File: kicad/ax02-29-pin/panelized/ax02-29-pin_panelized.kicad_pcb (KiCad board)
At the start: 4 copper layers, 100 x 100 mm, 62 parts, among them CN1 Leafony Bus, J2 Conn_02x05_Top_Bottom, J3 Conn_02x05_Top_Bottom, J4 Conn_02x05_Top_Bottom

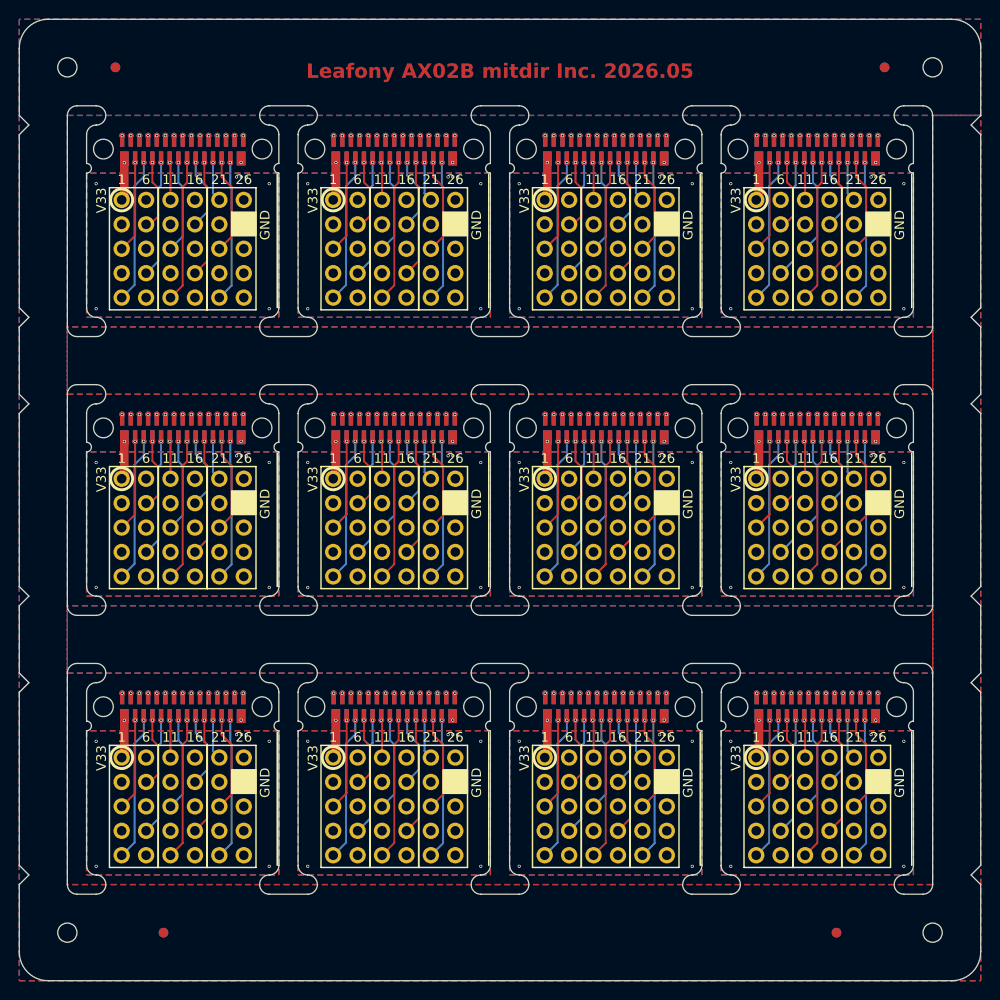
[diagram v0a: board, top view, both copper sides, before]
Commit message: 面付方法を変更
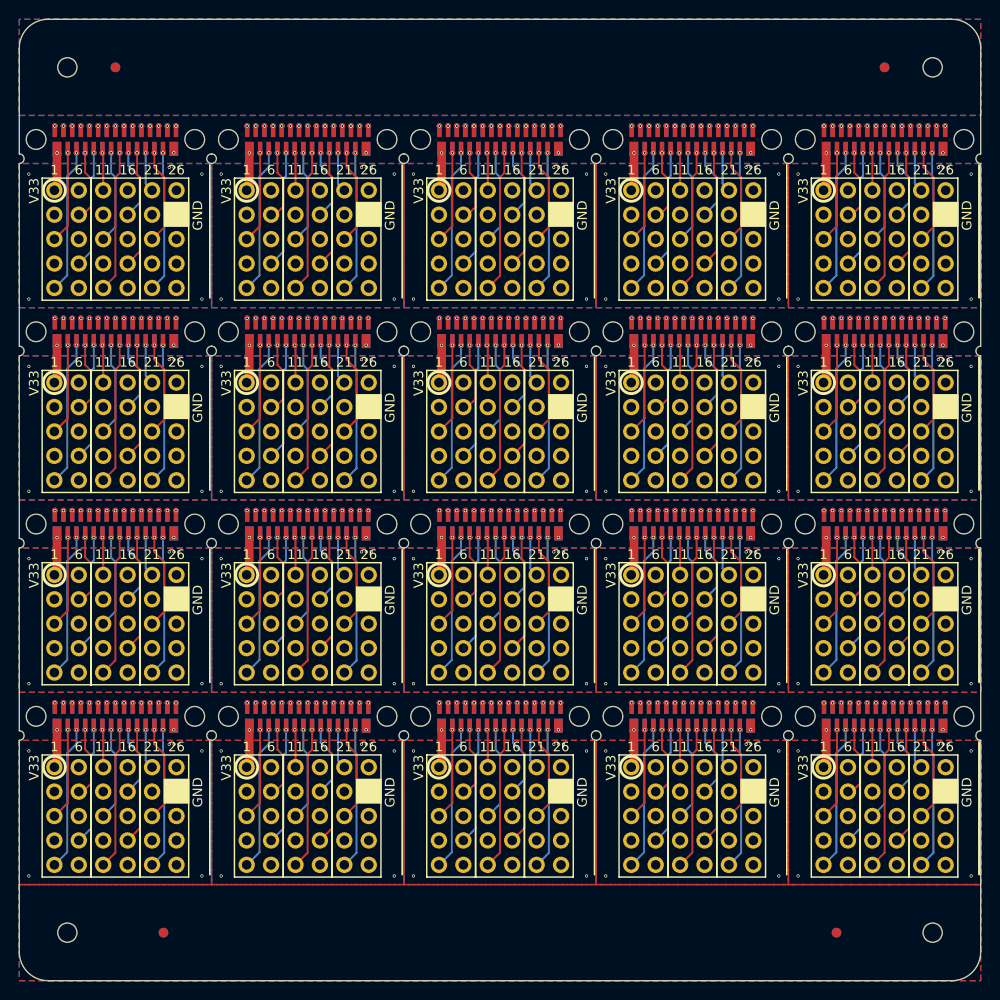
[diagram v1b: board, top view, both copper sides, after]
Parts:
- removed the CN1 at (83.6, 105.3)
- removed the CN1 at (39.6, 105.3)
- removed the CN1 at (105.6, 105.3)
- removed the CN1 at (105.6, 47.3)
- removed the CN1 at (39.6, 76.3)
- removed the CN1 at (61.6, 76.3)
- removed the CN1 at (83.6, 47.3)
- removed the CN1 at (61.6, 105.3)
- removed the CN1 at (83.6, 76.3)
- removed the CN1 at (61.6, 47.3)
- removed the CN1 at (39.6, 47.3)
- removed the CN1 at (105.6, 76.3)
- removed the J2 at (105.3, 109.6)
- removed the J2 at (105.3, 51.6)
- removed the J2 at (39.3, 80.6)
- removed the J2 at (39.3, 109.6)
- removed the J2 at (61.3, 109.6)
- removed the J2 at (83.3, 80.6)
- removed the J2 at (83.3, 109.6)
- removed the J2 at (39.3, 51.6)
- removed the J2 at (61.3, 51.6)
- removed the J2 at (83.3, 51.6)
- removed the J2 at (61.3, 80.6)
- removed the J2 at (105.3, 80.6)
- removed the J3 at (44.4, 80.6)
- removed the J3 at (88.4, 109.6)
- removed the J3 at (110.4, 80.6)
- removed the J3 at (110.4, 51.6)
- removed the J3 at (88.4, 80.6)
- removed the J3 at (66.4, 80.6)
- removed the J3 at (110.4, 109.6)
- removed the J3 at (66.4, 51.6)
- removed the J3 at (66.4, 109.6)
- removed the J3 at (88.4, 51.6)
- removed the J3 at (44.4, 109.6)
- removed the J3 at (44.4, 51.6)
- removed the J4 at (71.5, 80.6)
- removed the J4 at (115.5, 109.6)
- removed the J4 at (71.5, 109.6)
- removed the J4 at (115.5, 51.6)
- removed the J4 at (93.5, 109.6)
- removed the J4 at (49.5, 51.6)
- removed the J4 at (49.5, 109.6)
- removed the J4 at (71.5, 51.6)
- removed the J4 at (93.5, 51.6)
- removed the J4 at (93.5, 80.6)
- removed the J4 at (115.5, 80.6)
- removed the J4 at (49.5, 80.6)
- added CN1: Leafony Bus, Leafony:CN_F29_B29, F.Cu at (32.6, 66.3)
- added CN1: Leafony Bus, Leafony:CN_F29_B29, F.Cu at (112.6, 86.3)
- added CN1: Leafony Bus, Leafony:CN_F29_B29, F.Cu at (112.6, 46.3)
- added CN1: Leafony Bus, Leafony:CN_F29_B29, F.Cu at (32.6, 46.3)
- added CN1: Leafony Bus, Leafony:CN_F29_B29, F.Cu at (72.6, 106.3)
- added CN1: Leafony Bus, Leafony:CN_F29_B29, F.Cu at (72.6, 66.3)
- added CN1: Leafony Bus, Leafony:CN_F29_B29, F.Cu at (52.6, 86.3)
- added CN1: Leafony Bus, Leafony:CN_F29_B29, F.Cu at (92.6, 46.3)
- added CN1: Leafony Bus, Leafony:CN_F29_B29, F.Cu at (112.6, 66.3)
- added CN1: Leafony Bus, Leafony:CN_F29_B29, F.Cu at (92.6, 86.3)
- added CN1: Leafony Bus, Leafony:CN_F29_B29, F.Cu at (92.6, 66.3)
- added CN1: Leafony Bus, Leafony:CN_F29_B29, F.Cu at (32.6, 106.3)
- added CN1: Leafony Bus, Leafony:CN_F29_B29, F.Cu at (92.6, 106.3)
- added CN1: Leafony Bus, Leafony:CN_F29_B29, F.Cu at (52.6, 46.3)
- added CN1: Leafony Bus, Leafony:CN_F29_B29, F.Cu at (72.6, 46.3)
- added CN1: Leafony Bus, Leafony:CN_F29_B29, F.Cu at (112.6, 106.3)
- added CN1: Leafony Bus, Leafony:CN_F29_B29, F.Cu at (52.6, 66.3)
- added CN1: Leafony Bus, Leafony:CN_F29_B29, F.Cu at (32.6, 86.3)
- added CN1: Leafony Bus, Leafony:CN_F29_B29, F.Cu at (72.6, 86.3)
- added CN1: Leafony Bus, Leafony:CN_F29_B29, F.Cu at (52.6, 106.3)
- added J2: Conn_02x05_Top_Bottom, Leafony:PinHeader_2x05_2.54mm, F.Cu at (72.3, 110.6)
- added J2: Conn_02x05_Top_Bottom, Leafony:PinHeader_2x05_2.54mm, F.Cu at (52.3, 110.6)
- added J2: Conn_02x05_Top_Bottom, Leafony:PinHeader_2x05_2.54mm, F.Cu at (112.3, 50.6)
- added J2: Conn_02x05_Top_Bottom, Leafony:PinHeader_2x05_2.54mm, F.Cu at (92.3, 70.6)
- added J2: Conn_02x05_Top_Bottom, Leafony:PinHeader_2x05_2.54mm, F.Cu at (52.3, 70.6)
- added J2: Conn_02x05_Top_Bottom, Leafony:PinHeader_2x05_2.54mm, F.Cu at (112.3, 110.6)
- added J2: Conn_02x05_Top_Bottom, Leafony:PinHeader_2x05_2.54mm, F.Cu at (112.3, 70.6)
- added J2: Conn_02x05_Top_Bottom, Leafony:PinHeader_2x05_2.54mm, F.Cu at (52.3, 90.6)
- added J2: Conn_02x05_Top_Bottom, Leafony:PinHeader_2x05_2.54mm, F.Cu at (92.3, 90.6)
- added J2: Conn_02x05_Top_Bottom, Leafony:PinHeader_2x05_2.54mm, F.Cu at (52.3, 50.6)
- added J2: Conn_02x05_Top_Bottom, Leafony:PinHeader_2x05_2.54mm, F.Cu at (32.3, 110.6)
- added J2: Conn_02x05_Top_Bottom, Leafony:PinHeader_2x05_2.54mm, F.Cu at (72.3, 70.6)
- added J2: Conn_02x05_Top_Bottom, Leafony:PinHeader_2x05_2.54mm, F.Cu at (92.3, 110.6)
- added J2: Conn_02x05_Top_Bottom, Leafony:PinHeader_2x05_2.54mm, F.Cu at (72.3, 90.6)
- added J2: Conn_02x05_Top_Bottom, Leafony:PinHeader_2x05_2.54mm, F.Cu at (72.3, 50.6)
- added J2: Conn_02x05_Top_Bottom, Leafony:PinHeader_2x05_2.54mm, F.Cu at (112.3, 90.6)
- added J2: Conn_02x05_Top_Bottom, Leafony:PinHeader_2x05_2.54mm, F.Cu at (32.3, 70.6)
- added J2: Conn_02x05_Top_Bottom, Leafony:PinHeader_2x05_2.54mm, F.Cu at (92.3, 50.6)
- added J2: Conn_02x05_Top_Bottom, Leafony:PinHeader_2x05_2.54mm, F.Cu at (32.3, 50.6)
- added J2: Conn_02x05_Top_Bottom, Leafony:PinHeader_2x05_2.54mm, F.Cu at (32.3, 90.6)
- added J3: Conn_02x05_Top_Bottom, Leafony:PinHeader_2x05_2.54mm, F.Cu at (97.4, 110.6)
- added J3: Conn_02x05_Top_Bottom, Leafony:PinHeader_2x05_2.54mm, F.Cu at (97.4, 90.6)
- added J3: Conn_02x05_Top_Bottom, Leafony:PinHeader_2x05_2.54mm, F.Cu at (77.4, 50.6)
- added J3: Conn_02x05_Top_Bottom, Leafony:PinHeader_2x05_2.54mm, F.Cu at (117.4, 110.6)
- added J3: Conn_02x05_Top_Bottom, Leafony:PinHeader_2x05_2.54mm, F.Cu at (37.4, 90.6)
- added J3: Conn_02x05_Top_Bottom, Leafony:PinHeader_2x05_2.54mm, F.Cu at (37.4, 50.6)
- added J3: Conn_02x05_Top_Bottom, Leafony:PinHeader_2x05_2.54mm, F.Cu at (117.4, 90.6)
- added J3: Conn_02x05_Top_Bottom, Leafony:PinHeader_2x05_2.54mm, F.Cu at (77.4, 90.6)
- added J3: Conn_02x05_Top_Bottom, Leafony:PinHeader_2x05_2.54mm, F.Cu at (77.4, 70.6)
- added J3: Conn_02x05_Top_Bottom, Leafony:PinHeader_2x05_2.54mm, F.Cu at (57.4, 70.6)
- added J3: Conn_02x05_Top_Bottom, Leafony:PinHeader_2x05_2.54mm, F.Cu at (57.4, 90.6)
- added J3: Conn_02x05_Top_Bottom, Leafony:PinHeader_2x05_2.54mm, F.Cu at (97.4, 50.6)
- added J3: Conn_02x05_Top_Bottom, Leafony:PinHeader_2x05_2.54mm, F.Cu at (37.4, 70.6)
- added J3: Conn_02x05_Top_Bottom, Leafony:PinHeader_2x05_2.54mm, F.Cu at (77.4, 110.6)
- added J3: Conn_02x05_Top_Bottom, Leafony:PinHeader_2x05_2.54mm, F.Cu at (37.4, 110.6)
- added J3: Conn_02x05_Top_Bottom, Leafony:PinHeader_2x05_2.54mm, F.Cu at (97.4, 70.6)
- added J3: Conn_02x05_Top_Bottom, Leafony:PinHeader_2x05_2.54mm, F.Cu at (117.4, 50.6)
- added J3: Conn_02x05_Top_Bottom, Leafony:PinHeader_2x05_2.54mm, F.Cu at (57.4, 110.6)
- added J3: Conn_02x05_Top_Bottom, Leafony:PinHeader_2x05_2.54mm, F.Cu at (57.4, 50.6)
- added J3: Conn_02x05_Top_Bottom, Leafony:PinHeader_2x05_2.54mm, F.Cu at (117.4, 70.6)
- added J4: Conn_02x05_Top_Bottom, Leafony:PinHeader_2x05_2.54mm, F.Cu at (102.5, 50.6)
- added J4: Conn_02x05_Top_Bottom, Leafony:PinHeader_2x05_2.54mm, F.Cu at (62.5, 50.6)
- added J4: Conn_02x05_Top_Bottom, Leafony:PinHeader_2x05_2.54mm, F.Cu at (42.5, 90.6)
- added J4: Conn_02x05_Top_Bottom, Leafony:PinHeader_2x05_2.54mm, F.Cu at (82.5, 110.6)
- added J4: Conn_02x05_Top_Bottom, Leafony:PinHeader_2x05_2.54mm, F.Cu at (82.5, 50.6)
- added J4: Conn_02x05_Top_Bottom, Leafony:PinHeader_2x05_2.54mm, F.Cu at (122.5, 70.6)
- added J4: Conn_02x05_Top_Bottom, Leafony:PinHeader_2x05_2.54mm, F.Cu at (62.5, 90.6)
- added J4: Conn_02x05_Top_Bottom, Leafony:PinHeader_2x05_2.54mm, F.Cu at (42.5, 70.6)
- added J4: Conn_02x05_Top_Bottom, Leafony:PinHeader_2x05_2.54mm, F.Cu at (82.5, 90.6)
- added J4: Conn_02x05_Top_Bottom, Leafony:PinHeader_2x05_2.54mm, F.Cu at (62.5, 110.6)
- added J4: Conn_02x05_Top_Bottom, Leafony:PinHeader_2x05_2.54mm, F.Cu at (122.5, 90.6)
- added J4: Conn_02x05_Top_Bottom, Leafony:PinHeader_2x05_2.54mm, F.Cu at (102.5, 90.6)
- added J4: Conn_02x05_Top_Bottom, Leafony:PinHeader_2x05_2.54mm, F.Cu at (102.5, 70.6)
- added J4: Conn_02x05_Top_Bottom, Leafony:PinHeader_2x05_2.54mm, F.Cu at (122.5, 50.6)
- added J4: Conn_02x05_Top_Bottom, Leafony:PinHeader_2x05_2.54mm, F.Cu at (62.5, 70.6)
- added J4: Conn_02x05_Top_Bottom, Leafony:PinHeader_2x05_2.54mm, F.Cu at (82.5, 70.6)
- added J4: Conn_02x05_Top_Bottom, Leafony:PinHeader_2x05_2.54mm, F.Cu at (42.5, 50.6)
- added J4: Conn_02x05_Top_Bottom, Leafony:PinHeader_2x05_2.54mm, F.Cu at (42.5, 110.6)
- added J4: Conn_02x05_Top_Bottom, Leafony:PinHeader_2x05_2.54mm, F.Cu at (102.5, 110.6)
- added J4: Conn_02x05_Top_Bottom, Leafony:PinHeader_2x05_2.54mm, F.Cu at (122.5, 110.6)
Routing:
- net /F20: track 212.2 -> 353.6 mm, vias 12 -> 20
- net /F10: track 209.2 -> 348.6 mm, vias 12 -> 20
- net /F29: track 188.2 -> 313.7 mm, vias 12 -> 20
- net /F24: track 185.2 -> 308.7 mm, vias 12 -> 20
- net /F14: track 182.5 -> 304.1 mm, vias 12 -> 20
- net /F4: track 180.7 -> 301.2 mm, vias 12 -> 20
- net /F5: track 179.9 -> 299.8 mm, vias 12 -> 20
- net /F15: track 177.1 -> 295.2 mm, vias 12 -> 20
- net /F25: track 175.4 -> 292.4 mm, vias 12 -> 20
- net /F28: track 165.0 -> 275.1 mm, vias 12 -> 20
- net /F18: track 158.7 -> 264.4 mm, vias 12 -> 20
- net /F8: track 152.4 -> 254.0 mm, vias 12 -> 20
- net /F19: track 145.9 -> 243.1 mm, vias 12 -> 20
- net /F9: track 145.7 -> 242.9 mm, vias 12 -> 20
- net /F22: track 128.8 -> 214.6 mm, vias 12 -> 20
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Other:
- outline, holes or cut-outs redrawn
- board text removed: "Leafony AX02B mitdir Inc. 2026.05"
